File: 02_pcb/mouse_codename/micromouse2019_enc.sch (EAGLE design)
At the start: 7 parts, among them IC1 AS5047D

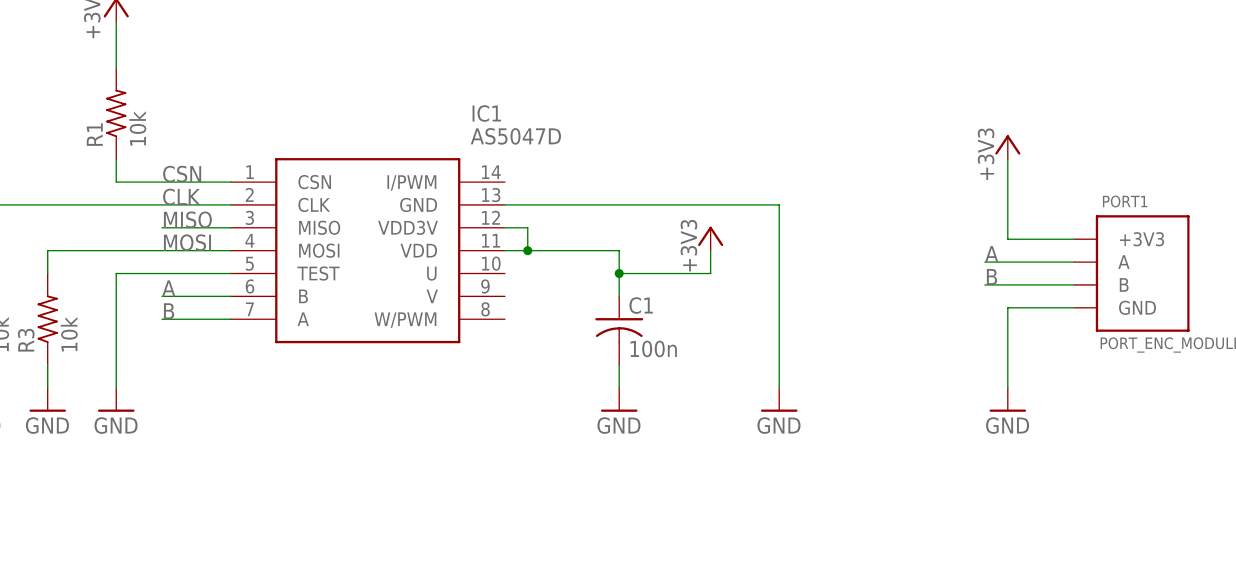
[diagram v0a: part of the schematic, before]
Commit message: ENC A B channels repaired
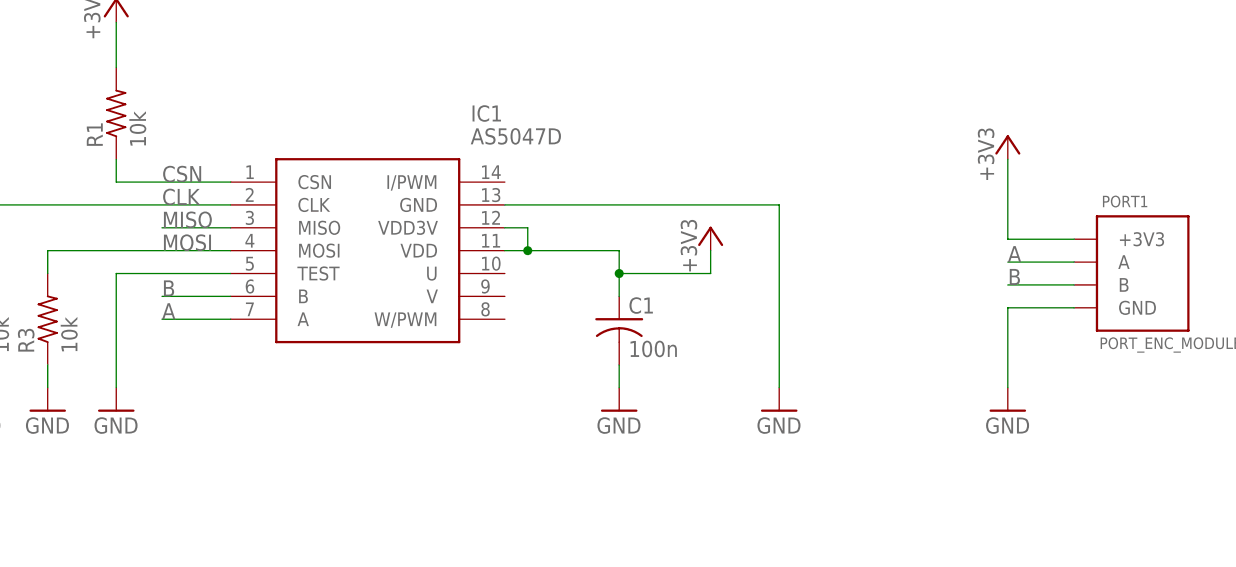
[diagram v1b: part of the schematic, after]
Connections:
- net A: now also IC1.A; no longer IC1.B
- net B: now also IC1.B; no longer IC1.A
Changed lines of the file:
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@@
 <setting verticaltext="up"/>
 </settings>
-<grid distance="0.1" unitdist="inch" unit="inch" style="lines" multiple="1" display="no" altdistance="0.01" altunitdist="inch" altunit="inch"/>
+<grid distance="0.05" unitdist="inch" unit="inch" style="lines" multiple="1" display="no" altdistance="0.01" altunitdist="inch" altunit="inch"/>
 <layers>
 <layer number="1" name="Top" color="4" fill="1" visible="no" active="no"/>
@@
 </segment>
 </net>
-<net name="A" class="0">
+<net name="B" class="0">
 <segment>
 <pinref part="IC1" gate="G$1" pin="B"/>
@@
 </segment>
 <segment>
-<wire x1="182.626" y1="100.33" x2="172.72" y2="100.33" width="0.1524" layer="91"/>
-<label x="172.72" y="100.33" size="1.778" layer="95"/>
-<pinref part="PORT1" gate="G$1" pin="A"/>
-</segment>
-</net>
-<net name="B" class="0">
+<pinref part="PORT1" gate="G$1" pin="B"/>
+<wire x1="182.626" y1="97.79" x2="175.26" y2="97.79" width="0.1524" layer="91"/>
+<label x="175.26" y="97.79" size="1.778" layer="95"/>
+</segment>
+</net>
+<net name="A" class="0">
 <segment>
 <pinref part="IC1" gate="G$1" pin="A"/>
@@
 </segment>
 <segment>
-<wire x1="182.626" y1="97.79" x2="172.72" y2="97.79" width="0.1524" layer="91"/>
-<label x="172.72" y="97.79" size="1.778" layer="95"/>
-<pinref part="PORT1" gate="G$1" pin="B"/>
-</segment>
-</net>
+<pinref part="PORT1" gate="G$1" pin="A"/>
+<wire x1="182.626" y1="100.33" x2="175.26" y2="100.33" width="0.1524" layer="91"/>
+<label x="175.26" y="100.33" size="1.778" layer="95"/>
+</segment>
+</net>
